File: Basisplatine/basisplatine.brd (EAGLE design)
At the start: 146 x 84.8 mm, 115 parts, among them IC1 RASPBERRY_PI_ZERO_W__V1.3_, IC2 MEGA8-AI, IC3 DIO5158XS8, IC4 TPS613222ADBVR, IC5 AP63205WU-7, J1 DCJ0202, J2 54601-908WPLF, J3 54601-908WPLF, J4 54601-908WPLF, J5 54601-908WPLF, J6 54601-908WPLF, Q2 NTF5P03T3G

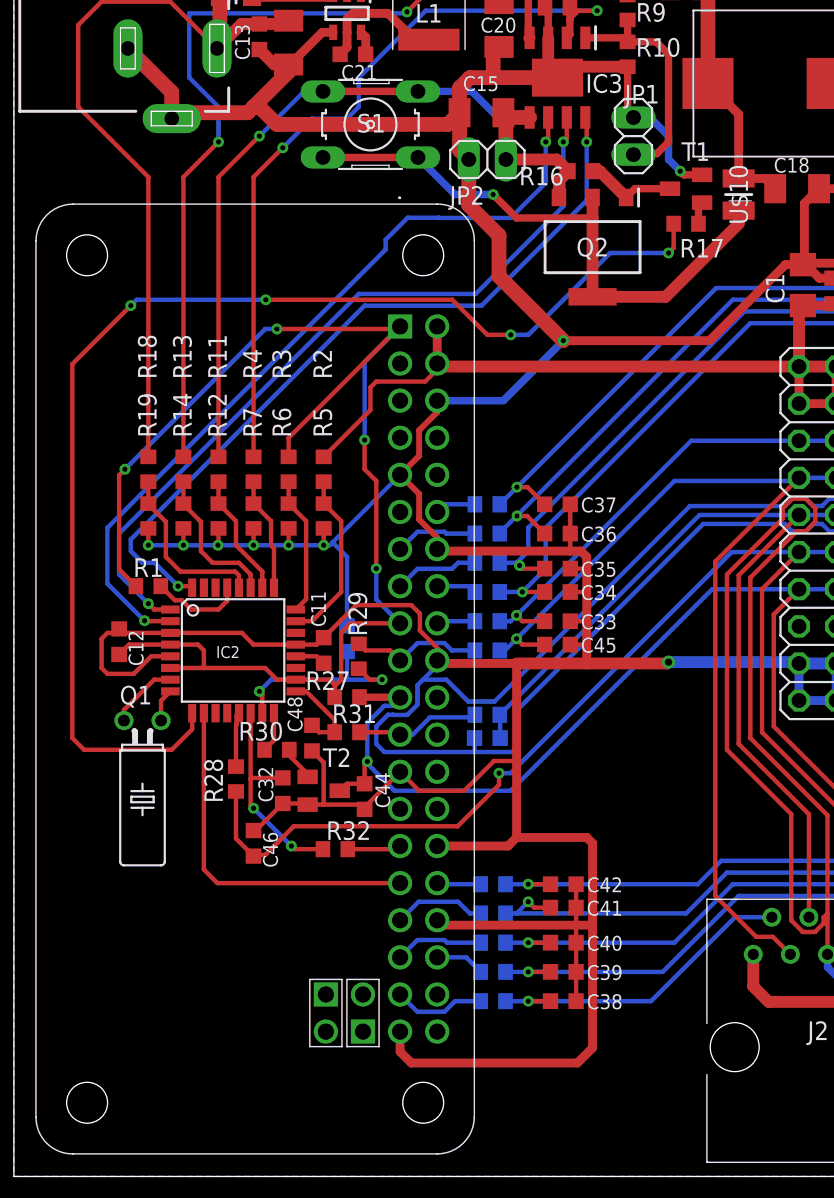
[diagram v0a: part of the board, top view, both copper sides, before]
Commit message: Added Stueckliste, Taster, LED
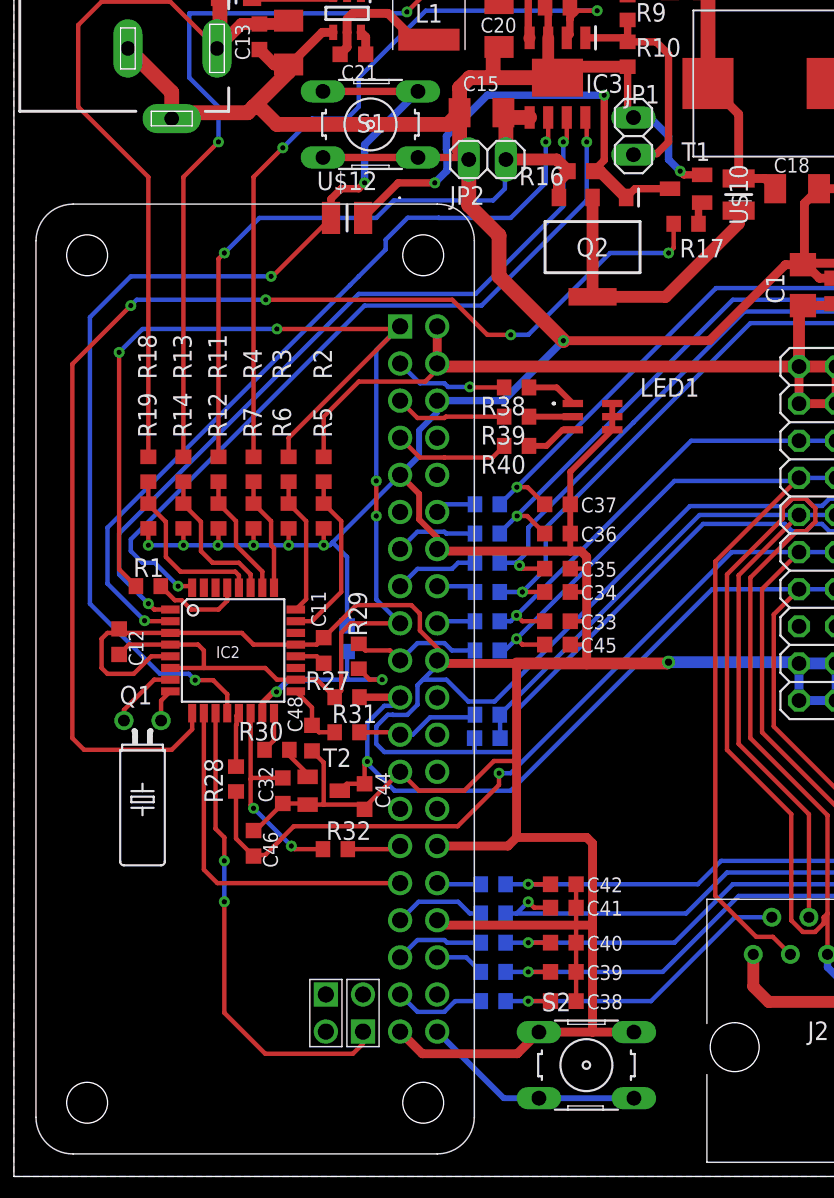
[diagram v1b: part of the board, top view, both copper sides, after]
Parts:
- added LED1: ASMB-UTF0-0D20B, basisplatine_lib:ASMBUTF00D20B
- added R38, R39, R40: 100R, rcl:R0603
- added S2: (no value), switch-omron:B3F-10XX
- added U$12: SK1035-TP, basisplatine_lib:INDC2520X120N
- C1, C22: value (none) -> 10u
- C18, C2, C23, C24, C25, C26, C3, C4, C5: value 2u2 -> 10u
- R11, R13, R2, R3: value (none) -> 82k
- R12, R14, R19, R4, R5, R6, R7: value (none) -> 10k
- R18: value (none) -> 270k
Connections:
- net SHUTDOWN renamed RUNNING
- removed net N$10: Q2.1, R16.2, T1.C
- new net LED_BLUE: IC1.7, R40.2
- new net LED_GREEN: IC1.5, R39.2
- new net LED_RED: IC1.3, R38.2
- new net N$21: IC1.40, S2.3, S2.4
- new net N$23: Q2.1, R16.2, T1.C, U$12.1
- new net N$30: LED1.1, R38.1
- new net N$31: LED1.3, R39.1
- new net N$32: LED1.5, R40.1
- new net RESET_PI: IC1.41, IC2.11
- new net START_STOPBUTTON: IC2.12, S1.3, S1.4, U$12.2
- net GND: now also LED1.2, LED1.4, LED1.6, S1.1, S1.2, S2.1, S2.2
- net N$12: no longer S1.1, S1.2
- net VBAT: no longer S1.3, S1.4
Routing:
- net START_STOPBUTTON: track 0.00 -> 70.5 mm, vias 0 -> 3
- net N$23: track 0.00 -> 33.2 mm, vias 0 -> 2
- net RESET_PI: track 0.00 -> 32.5 mm, vias 0 -> 2
- net GND: track 1419.7 -> 1441.9 mm
- net N$12: track 39.9 -> 19.8 mm, vias 1 -> 0
- net N$21: track 0.00 -> 15.3 mm
- net LED_BLUE: track 0.00 -> 8.01 mm
- net LED_RED: track 0.00 -> 7.80 mm, vias 0 -> 1
- net LED_GREEN: track 0.00 -> 7.65 mm
- net VBAT: track 56.4 -> 49.2 mm
- net N$10: track 6.24 -> 0.00 mm
- net +3V3: track 93.8 -> 98.4 mm
- net N$32: track 0.00 -> 3.46 mm
- net N$30: track 0.00 -> 3.46 mm
- net N$31: track 0.00 -> 3.00 mm
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
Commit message: Added 3,3V and vias to Basisplatine, ...
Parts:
- removed U$7: SK1035-TP, basisplatine_lib:INDC2520X120N
- added C49, C50, C51, C52, C53, C54, C55, C56, C57, C58: 100n, rcl:C0603K
- added D1: SBRT10U50SP5-13, basisplatine_lib:SBRT10U50SP513
- moved C17 4.42 mm to (56.4, 82.0)
- moved R15 3.62 mm to (54.8, 82.0)
- moved C16 2.80 mm to (62.4, 67.2)
- moved IC4 2.80 mm to (60.4, 72.0)
- moved C26 2.40 mm to (141.2, 24.8)
- moved C31 2.40 mm to (141.2, 26.8)
- moved U$8 0.80 mm to (70.0, 74.8)
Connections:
- net +3V3: now also C49.1, C50.1, C51.1, C52.1, C53.1, C54.1, C55.1, C56.1, C57.1, C58.1, J2.8, J3.8, J4.8, J5.8, J6.8, U$1.15, U$1.16, U$2.15, U$2.16, U$3.15, U$3.16, U$4.15, U$4.16, U$5.15, U$5.16
- net GND: now also C49.2, C50.2, C51.2, C52.2, C53.2, C54.2, C55.2, C56.2, C57.2, C58.2; no longer J2.8, J3.8, J4.8, J5.8, J6.8
- net N$1: now also D1.1, D1.2; no longer U$7.1
- net N$8: now also D1.3; no longer U$7.2
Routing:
- net GND: track 1441.9 -> 860.3 mm, vias 9 -> 353
- net +3V3: track 98.4 -> 433.3 mm, vias 4 -> 10
- net N$1: track 8.63 -> 17.1 mm
- net N$8: track 14.0 -> 22.5 mm
- net N$7: track 2.41 -> 1.61 mm
- net +5V: track 537.9 -> 538.7 mm
